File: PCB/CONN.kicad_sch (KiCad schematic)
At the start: 12 parts, among them J1 mot0, J2 encoder0, J3 spare_pins, J4 UART0 DEBUG, U2 LD1117S33TR_SOT223, U5 USBLC6-2SC6

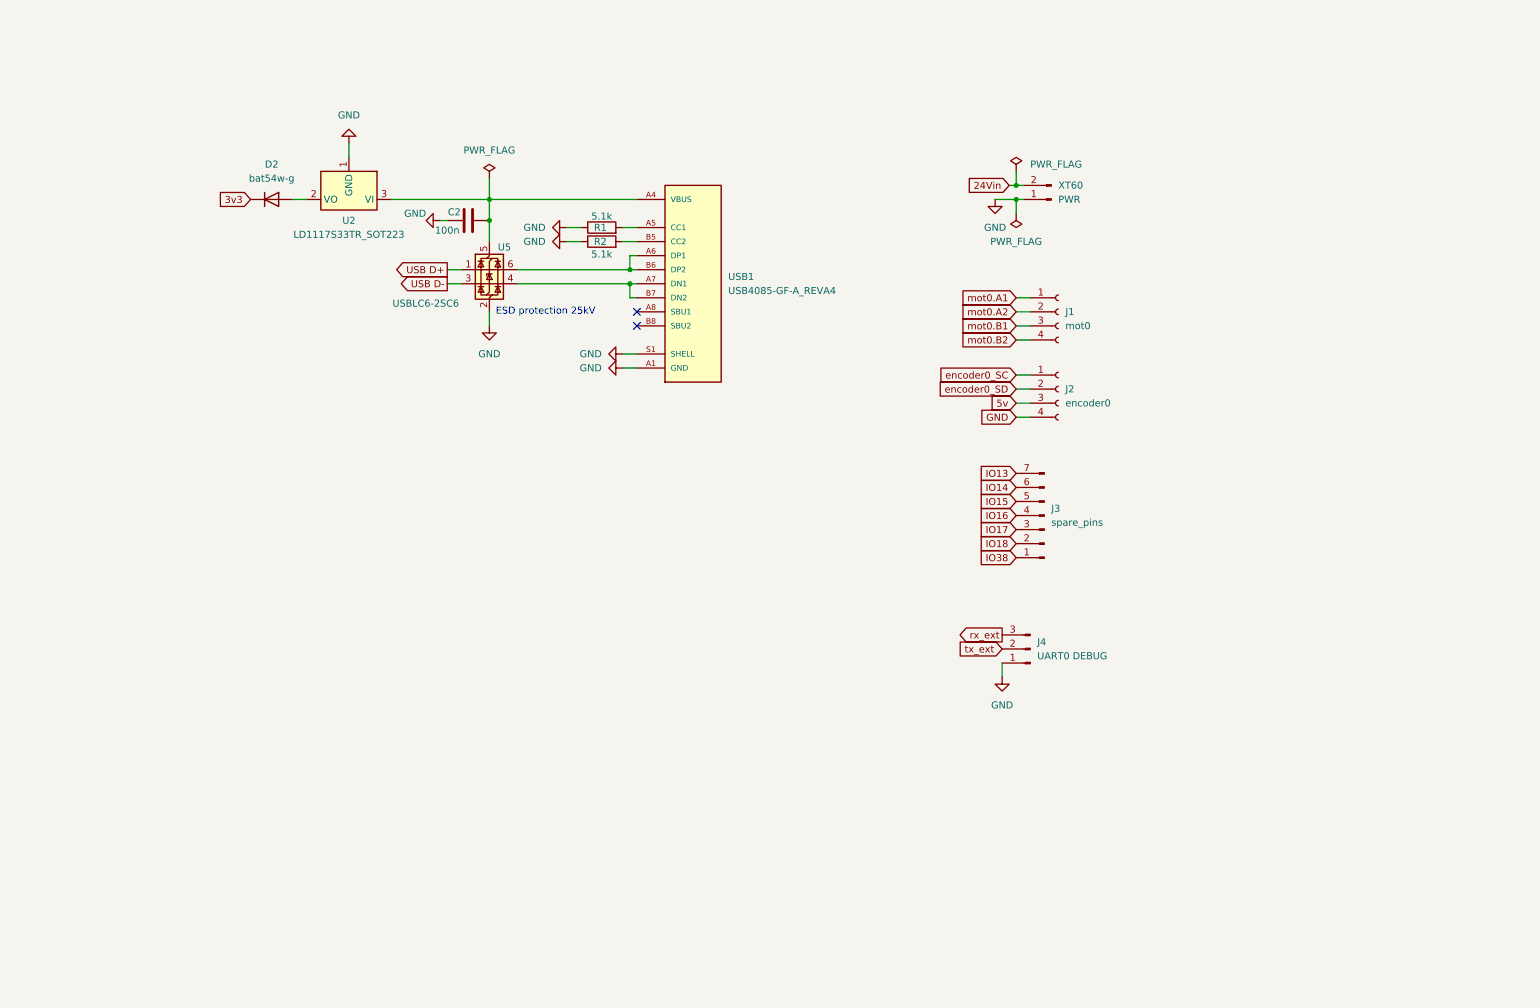
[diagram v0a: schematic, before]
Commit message: Fixed UART, cleaned schematic, improved LDO
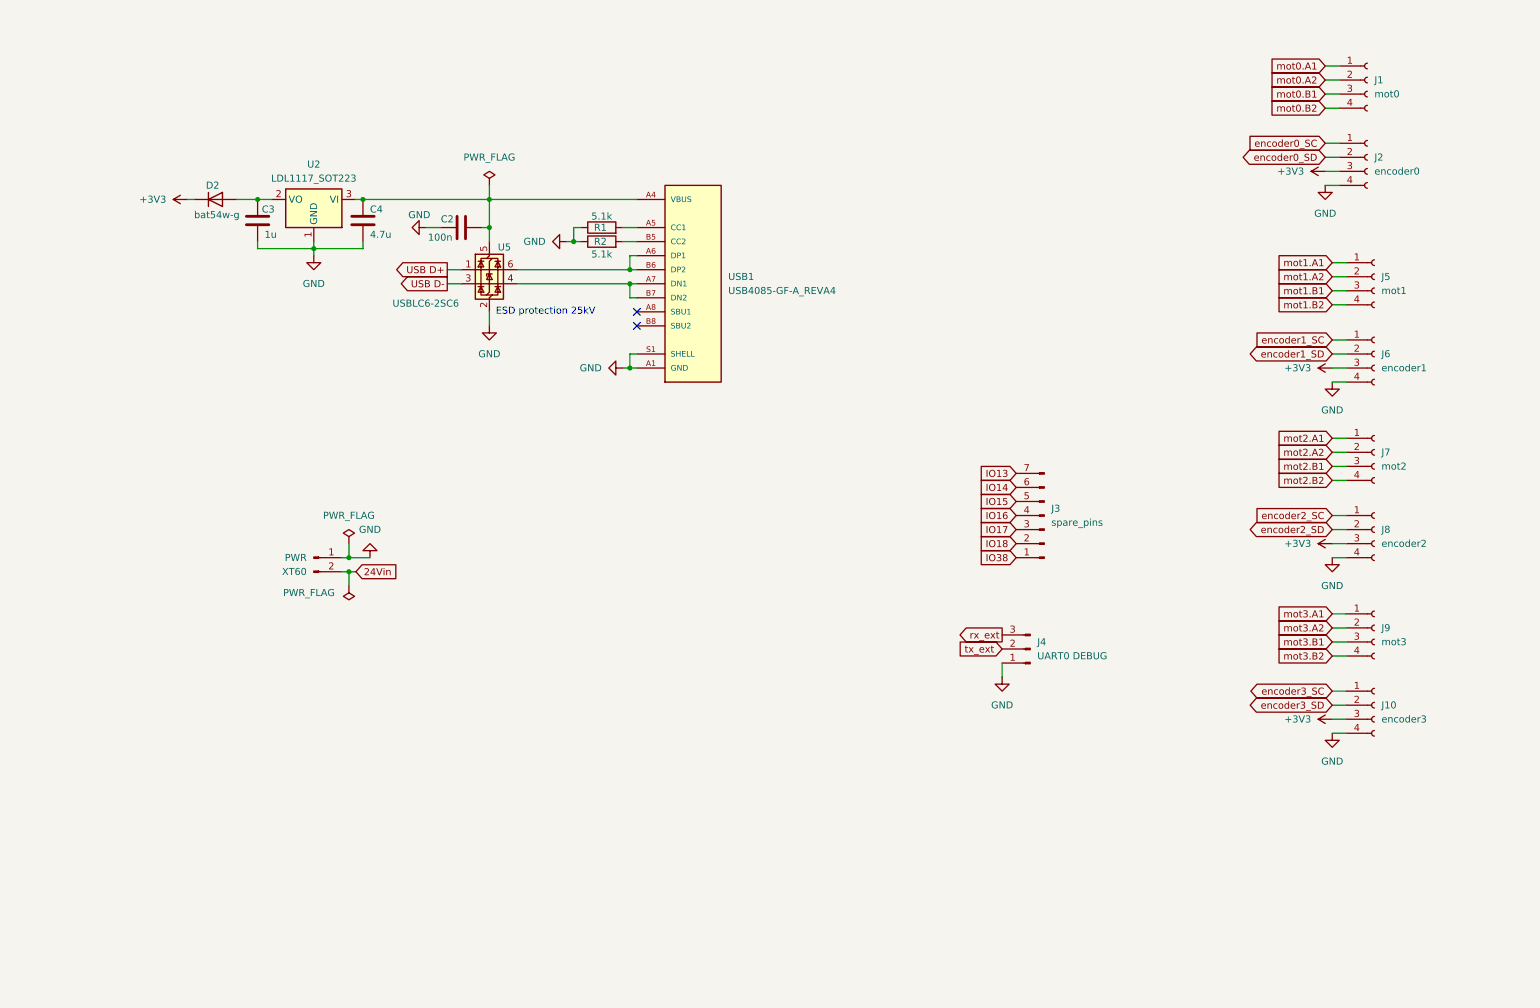
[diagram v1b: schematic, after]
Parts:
- added C3: 1u, symbol Device:C
- added C4: 4.7u, symbol Device:C
- added J10: encoder3, symbol Connector:Conn_01x04_Socket
- added J5: mot1, symbol Connector:Conn_01x04_Socket
- added J6: encoder1, symbol Connector:Conn_01x04_Socket
- added J7: mot2, symbol Connector:Conn_01x04_Socket
- added J8: encoder2, symbol Connector:Conn_01x04_Socket
- added J9: mot3, symbol Connector:Conn_01x04_Socket
- C2: footprint (none) -> Capacitor_SMD:C_0201_0603Metric_Pad0.64x0.40mm_HandSolder
- R1, R2: footprint (none) -> Resistor_SMD:R_0603_1608Metric_Pad0.98x0.95mm_HandSolder
- U2: value LD1117S33TR_SOT223 -> LDL1117_SOT223
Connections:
- net 5v is gone; now on net +3V3: J2.3 (Pin_3)
- net GND: now also C3.2, C4.2, J10.4 (Pin_4), J6.4 (Pin_4), J8.4 (Pin_4)
- net VBUS: now also C4.1
- net at D2.2 (A), U2.2 (VO): now also C3.1
- net 3v3 renamed +3V3
- net +3V3: now also J10.3 (Pin_3), J6.3 (Pin_3), J8.3 (Pin_3)
- new net encoder1_SC: J6.1 (Pin_1)
- new net encoder1_SD: J6.2 (Pin_2)
- new net encoder2_SC: J8.1 (Pin_1)
- new net encoder2_SD: J8.2 (Pin_2)
- new net encoder3_SC: J10.1 (Pin_1)
- new net encoder3_SD: J10.2 (Pin_2)
- new net mot1.A1: J5.1 (Pin_1)
- new net mot1.A2: J5.2 (Pin_2)
- new net mot1.B1: J5.3 (Pin_3)
- new net mot1.B2: J5.4 (Pin_4)
- new net mot2.A1: J7.1 (Pin_1)
- new net mot2.A2: J7.2 (Pin_2)
- new net mot2.B1: J7.3 (Pin_3)
- new net mot2.B2: J7.4 (Pin_4)
- new net mot3.A1: J9.1 (Pin_1)
- new net mot3.A2: J9.2 (Pin_2)
- new net mot3.B1: J9.3 (Pin_3)
- new net mot3.B2: J9.4 (Pin_4)
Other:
- moved on the sheet: C2, D2, J1, J2, U2, XT60

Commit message: PCB layout v1.0
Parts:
- removed J10: encoder3, symbol Connector:Conn_01x04_Socket
- removed J2: encoder0, symbol Connector:Conn_01x04_Socket
- removed J3: spare_pins, symbol Connector:Conn_01x07_Pin
- removed J6: encoder1, symbol Connector:Conn_01x04_Socket
- removed J8: encoder2, symbol Connector:Conn_01x04_Socket
- added FB1, FB2, FB3, FB4: FerriteBead, Inductor_SMD:L_0603_1608Metric_Pad1.05x0.95mm_HandSolder, symbol Device:FerriteBead
- added J1: Conn_01x02_Pin, Connector_PinHeader_2.54mm:PinHeader_1x02_P2.54mm_Vertical, symbol Connector:Conn_01x02_Pin
- added J4: spare, Connector_PinHeader_2.54mm:PinHeader_1x01_P2.54mm_Vertical, symbol Connector:Conn_01x01_Pin
- added R20, R21, R22, R31, R32, R33, R35, R36, R37, R39, R40, R41: 10R, Resistor_SMD:R_0603_1608Metric_Pad0.98x0.95mm_HandSolder, symbol Device:R
- added R29, R30, R34, R38: 10k, Resistor_SMD:R_0603_1608Metric_Pad0.98x0.95mm_HandSolder, symbol Device:R
- added TVS1, TVS10, TVS11, TVS12, TVS2, TVS3, TVS4, TVS5, TVS6, TVS7, TVS8, TVS9: CDSOD323-T05, Diode_SMD:D_SOD-323, symbol Diode:SD05_SOD323
- added encoder0, encoder1, encoder2, encoder3: JST-XH-AM 6pin, Connector_JST:JST_XH_B6B-XH-AM_1x06_P2.50mm_Vertical, symbol Connector:Conn_01x06_Socket
- C2: footprint Capacitor_SMD:C_0201_0603Metric_Pad0.64x0.40mm_HandSolder -> Capacitor_SMD:C_0603_1608Metric_Pad1.08x0.95mm_HandSolder
- C3, C4: footprint (none) -> Capacitor_SMD:C_0603_1608Metric_Pad1.08x0.95mm_HandSolder
- D2: value bat54w-g -> BAT54WG; footprint (none) -> Package_TO_SOT_SMD:SOT-323_SC-70_Handsoldering
- J5: renamed from J4; footprint (none) -> Connector_PinHeader_2.54mm:PinHeader_1x03_P2.54mm_Vertical
- USB1: footprint USB4085-GF-A_REVA4:GCT_USB4085-GF-A_REVA4 -> VNfootprints:GCT_USB4085-GF-A_REVA4
- barreljack1: renamed from XT60; footprint (none) -> Connector_BarrelJack:BarrelJack_CUI_PJ-063AH_Horizontal
- mot0: renamed from J1; value mot0 -> JST-XH-AM 4pin; footprint (none) -> Connector_JST:JST_XH_B4B-XH-AM_1x04_P2.50mm_Vertical
- mot1: renamed from J5; value mot1 -> JST-XH-AM 4pin; footprint (none) -> Connector_JST:JST_XH_B4B-XH-AM_1x04_P2.50mm_Vertical
- mot2: renamed from J7; value mot2 -> JST-XH-AM 4pin; footprint (none) -> Connector_JST:JST_XH_B4B-XH-AM_1x04_P2.50mm_Vertical
- mot3: renamed from J9; value mot3 -> JST-XH-AM 4pin; footprint (none) -> Connector_JST:JST_XH_B4B-XH-AM_1x04_P2.50mm_Vertical
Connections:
- net +3V3: now also FB1.1, FB2.1, FB3.1, FB4.1, R29.2, R30.2, R34.2, R38.2
- net GND: now also J1.1 (Pin_1), TVS1.1 (A1), TVS10.1 (A1), TVS11.1 (A1), TVS12.1 (A1), TVS2.1 (A1), TVS3.1 (A1), TVS4.1 (A1), TVS5.1 (A1), TVS6.1 (A1), TVS7.1 (A1), TVS8.1 (A1), TVS9.1 (A1), encoder0.4 (Pin_4), encoder0.5 (Pin_5), encoder1.4 (Pin_4), encoder1.5 (Pin_5), encoder2.4 (Pin_4), encoder2.5 (Pin_5), encoder3.4 (Pin_4), encoder3.5 (Pin_5)
- net IO38: now also J4.1 (Pin_1)
- net encoder0_SC: now also R20.1, TVS2.2 (A2)
- net encoder0_SD: now also R21.1, TVS1.2 (A2)
- net encoder1_SC: now also R31.1, TVS5.2 (A2)
- net encoder1_SD: now also R32.1, TVS4.2 (A2)
- net encoder2_SC: now also R35.1, TVS8.2 (A2)
- net encoder2_SD: now also R36.1, TVS7.2 (A2)
- net encoder3_SC: now also R39.1, TVS11.2 (A2)
- net encoder3_SD: now also R40.1, TVS10.2 (A2)
- net mot0.A1: now also mot0.2 (Pin_2); no longer mot0.1 (Pin_1)
- net mot0.A2: now also mot0.3 (Pin_3); no longer mot0.2 (Pin_2)
- net mot0.B1: now also mot0.1 (Pin_1); no longer mot0.3 (Pin_3)
- net mot1.A1: now also mot1.2 (Pin_2); no longer mot1.1 (Pin_1)
- net mot1.A2: now also mot1.3 (Pin_3); no longer mot1.2 (Pin_2)
- net mot1.B1: now also mot1.1 (Pin_1); no longer mot1.3 (Pin_3)
- net mot2.A1: now also mot2.2 (Pin_2); no longer mot2.1 (Pin_1)
- net mot2.A2: now also mot2.3 (Pin_3); no longer mot2.2 (Pin_2)
- net mot2.B1: now also mot2.1 (Pin_1); no longer mot2.3 (Pin_3)
- net mot3.A1: now also mot3.2 (Pin_2); no longer mot3.1 (Pin_1)
- net mot3.A2: now also mot3.3 (Pin_3); no longer mot3.2 (Pin_2)
- net mot3.B1: now also mot3.1 (Pin_1); no longer mot3.3 (Pin_3)
- net VO_USB_LDO: now reaches C3.1, D2.2 (A), U2.2 (VO)
- new net: R33.2, encoder1.6 (Pin_6)
- new net: FB4.2, encoder3.3 (Pin_3)
- new net: R21.2, encoder0.2 (Pin_2)
- new net: R22.2, encoder0.6 (Pin_6)
- new net: R20.2, encoder0.1 (Pin_1)
- new net: R41.2, encoder3.6 (Pin_6)
- new net: FB2.2, encoder1.3 (Pin_3)
- new net: R31.2, encoder1.1 (Pin_1)
- new net: R39.2, encoder3.1 (Pin_1)
- new net: R32.2, encoder1.2 (Pin_2)
- new net: R36.2, encoder2.2 (Pin_2)
- new net: R40.2, encoder3.2 (Pin_2)
- new net: R37.2, encoder2.6 (Pin_6)
- new net: R35.2, encoder2.1 (Pin_1)
- new net: FB1.2, encoder0.3 (Pin_3)
- new net: FB3.2, encoder2.3 (Pin_3)
- new net endswitch0: R22.1, R29.1, TVS3.2 (A2)
- new net endswitch1: R30.1, R33.1, TVS6.2 (A2)
- new net endswitch2: R34.1, R37.1, TVS9.2 (A2)
- new net endswitch3: R38.1, R41.1, TVS12.2 (A2)
- new net reset: J1.2 (Pin_2)
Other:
- moved on the sheet: C2, C3, C4, D2, J5, R1, R2, U2, U5, USB1, barreljack1, mot0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

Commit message: pcb version ready for final check
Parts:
- added J6: PWR_SWITCH, Connector_PinHeader_2.54mm:PinHeader_1x03_P2.54mm_Vertical, symbol Connector:Conn_01x03_Pin
- added fan1: Conn_01x02_Pin, Connector_PinHeader_2.54mm:PinHeader_1x02_P2.54mm_Vertical, symbol Connector:Conn_01x02_Pin
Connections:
- net 24Vin: now also J6.3 (Pin_3)
- net GND: now also fan1.1 (Pin_1)
- new net 24V: fan1.2 (Pin_2)
- new net PWRSWITCH_diode: J6.1 (Pin_1)
- new net PWRSWITCH_gate: J6.2 (Pin_2)
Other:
- note added: "in case of issue pwr switch can be bypassed by shorting gate and diode"

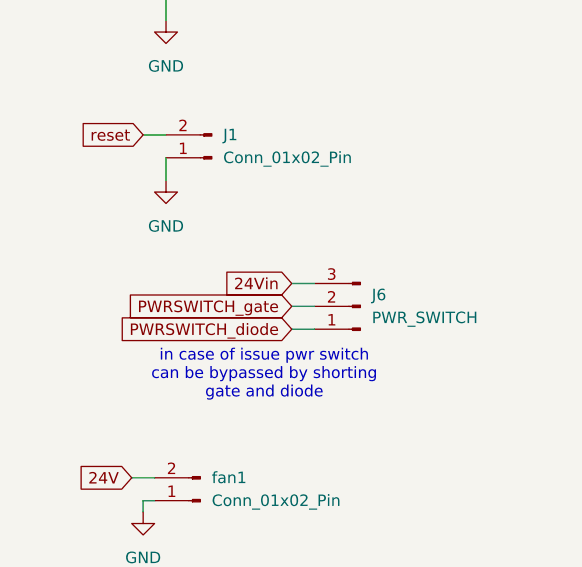
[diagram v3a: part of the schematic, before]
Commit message: [pcb] Final processing and export of production data
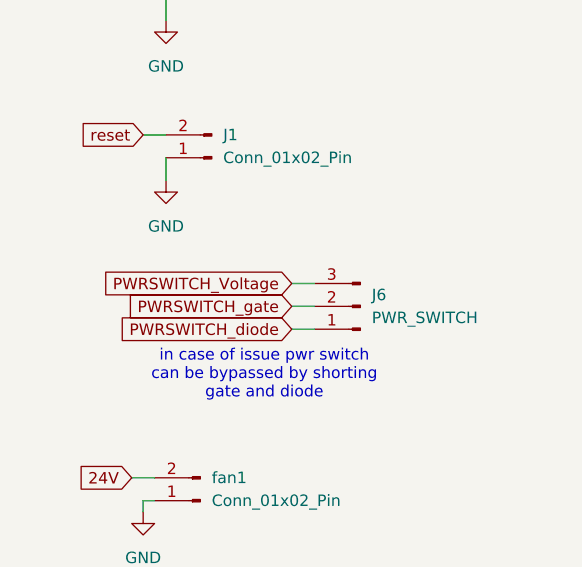
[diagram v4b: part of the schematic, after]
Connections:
- net 24Vin: no longer J6.3 (Pin_3)
- new net PWRSWITCH_Voltage: J6.3 (Pin_3)
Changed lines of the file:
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@@
 		)
 	)
-	(global_label "24Vin"
+	(global_label "PWRSWITCH_Voltage"
 		(shape input)
 		(at 43.18 127 180)
@@
 		)
 		(property "Intersheetrefs" "${INTERSHEET_REFS}"
-			(at 34.9334 127 0)
+			(at 21.3869 127 0)
 			(hide yes)
 			(show_name no)

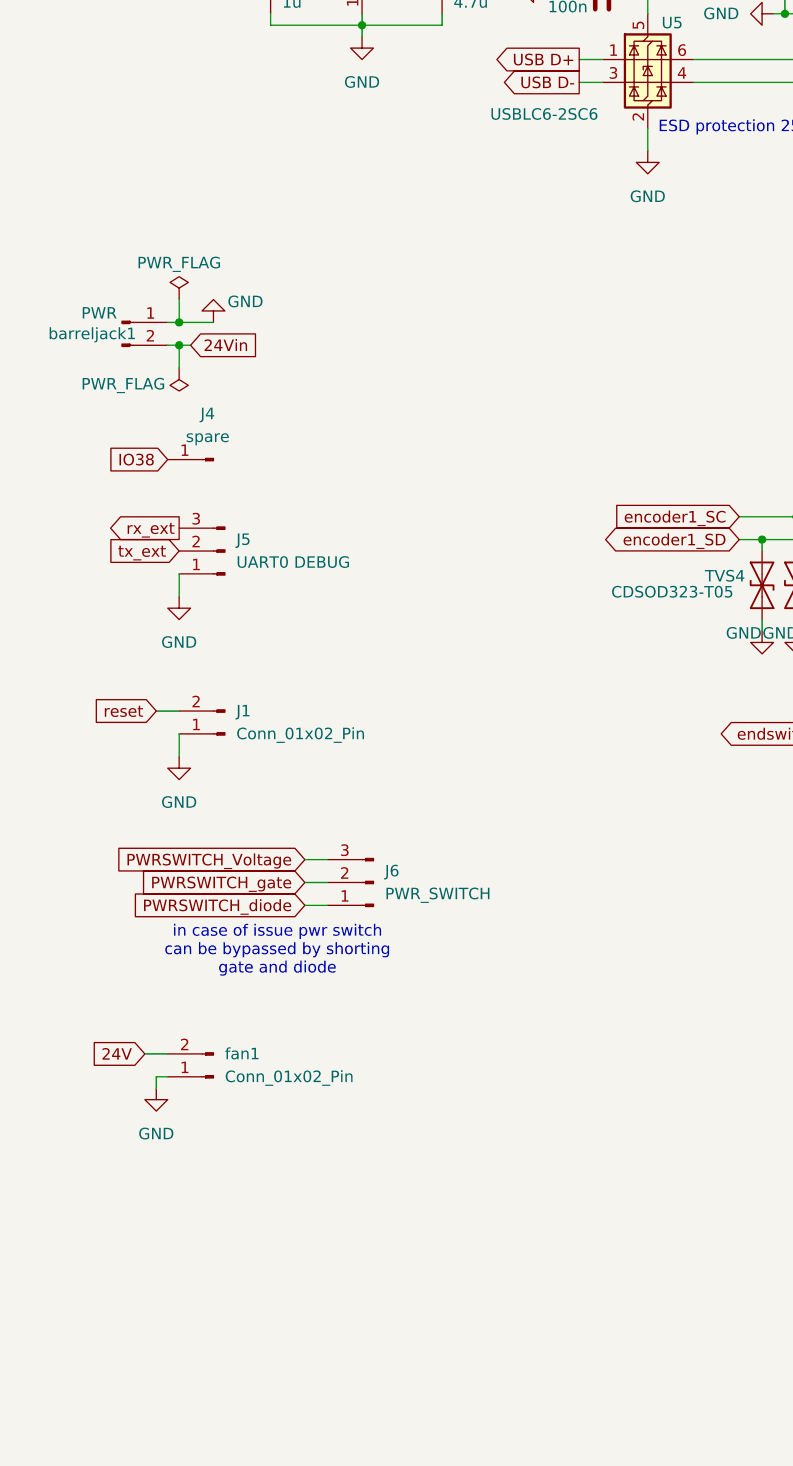
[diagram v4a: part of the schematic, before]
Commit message: Auto stash before merge of "main" and "origin/main"
[pcb] Updated main connector and LT8610AC layout
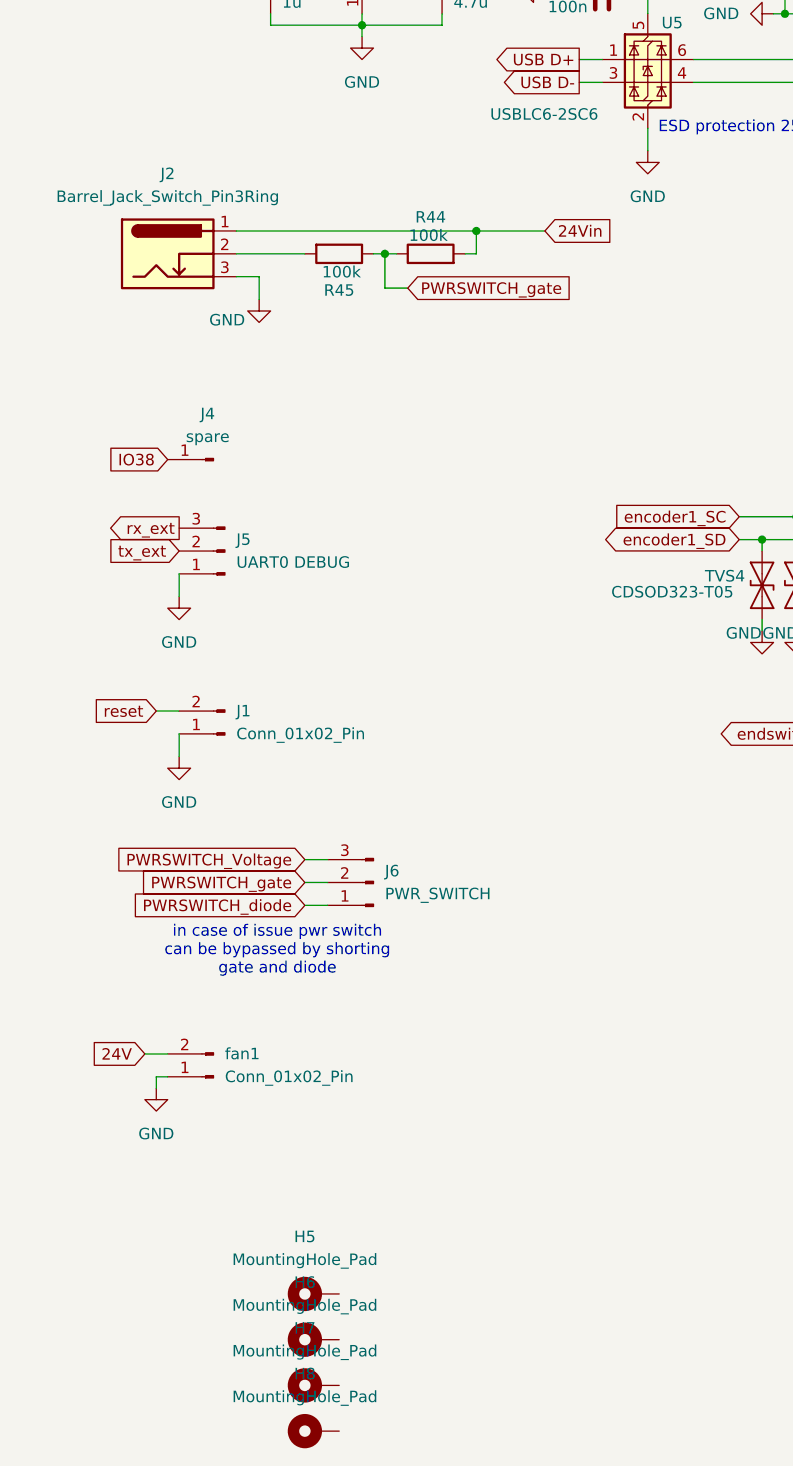
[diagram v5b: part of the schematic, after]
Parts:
- removed barreljack1: PWR, Connector_BarrelJack:BarrelJack_CUI_PJ-063AH_Horizontal, symbol Connector:Conn_01x02_Pin
- added H5, H6, H7, H8: MountingHole_Pad, MountingHole:MountingHole_3.2mm_M3_DIN965_Pad, symbol Mechanical:MountingHole_Pad
- added J2: Barrel_Jack_Switch_Pin3Ring, Connector_BarrelJack:BarrelJack_Wuerth_6941xx301002, symbol Connector:Barrel_Jack_Switch_Pin3Ring
- added R44, R45: 100k, Resistor_SMD:R_0603_1608Metric_Pad0.98x0.95mm_HandSolder, symbol Device:R
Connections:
- net 24Vin: now also J2.1, R44.2
- net GND: now also J2.3
- net PWRSWITCH_gate: now also R44.1, R45.1
- new net: J2.2, R45.2
